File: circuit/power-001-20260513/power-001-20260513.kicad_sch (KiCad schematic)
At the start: 57 parts, among them J1 VIN, J2 +5V_{Line}, J3 Power, J4 Logic, J5 Sub_{Power}, J6 Sub_{Signal}, Q1 BSS138, Q2 PMOS, SW1 SW_SPDT, SW2 SW_SPDT, SW3 SW_SPDT, SW4 Locker_SW, U1 OKL-T/6-W12N-C, U2 OKL-T/6-W12N-C, U3 AZ1084-3.3, U4 BP5293-33, U5 PIC12F683-xSN

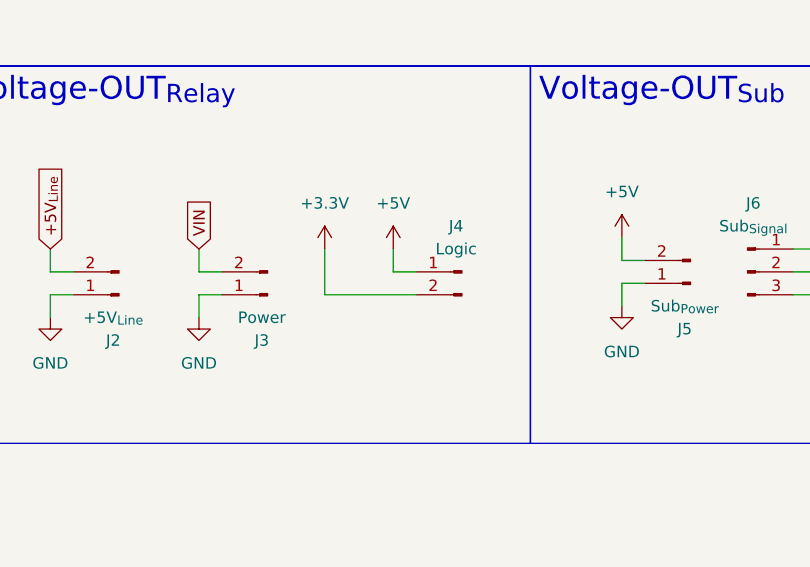
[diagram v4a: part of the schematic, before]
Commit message: Update 供給基板のXT30の向きを変更、それに伴う電源基板の回路図も変更
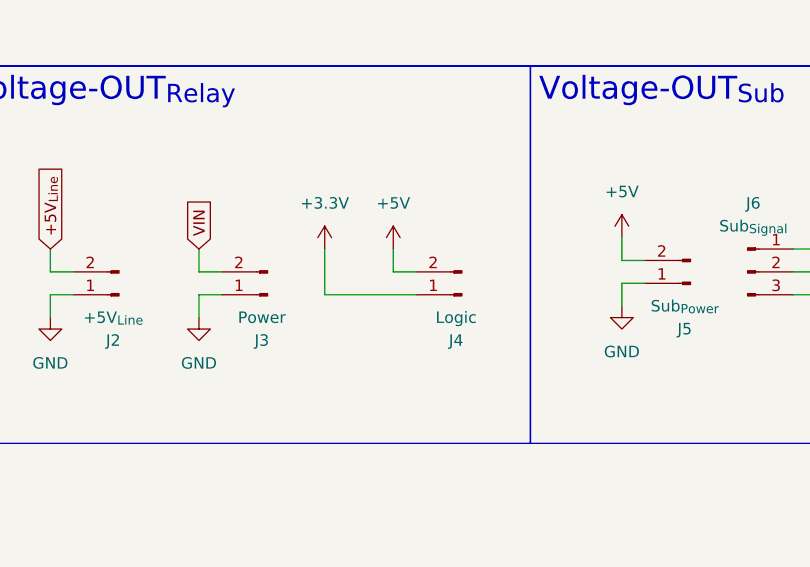
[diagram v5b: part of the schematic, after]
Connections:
- net +3.3V: now also J4.1 (Pin_1); no longer J4.2 (Pin_2)
- net +5V: now also J4.2 (Pin_2); no longer J4.1 (Pin_1)
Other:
- moved on the sheet: J4
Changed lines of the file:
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@@
 	(wire
 		(pts
+			(xy 172.72 121.92) (xy 182.88 121.92)
+		)
+		(stroke
+			(width 0)
+			(type default)
+		)
+	)
+	(wire
+		(pts
 			(xy 226.06 76.2) (xy 223.52 76.2)
 		)
@@
 	(wire
 		(pts
-			(xy 182.88 121.92) (xy 172.72 121.92)
-		)
-		(stroke
-			(width 0)
-			(type default)
-		)
-	)
-	(wire
-		(pts
 			(xy 20.32 125.73) (xy 22.86 125.73)
 		)
@@
 	(symbol
 		(lib_id "Connector:Conn_01x02_Pin")
-		(at 187.96 119.38 0)
-		(mirror y)
+		(at 187.96 121.92 180)
 		(unit 1)
 		(body_style 1)
@@
 		(dnp no)
 		(property "Reference" "J4"
-			(at 187.325 114.3 0)
+			(at 187.325 127 0)
 			(show_name no)
 			(do_not_autoplace no)
@@
 		)
 		(property "Value" "Logic"
-			(at 187.325 116.84 0)
+			(at 187.325 124.46 0)
 			(show_name no)
 			(do_not_autoplace no)
@@
 		)
 		(property "Footprint" "Connector_AMASS:AMASS_XT30PW-F_1x02_P2.50mm_Horizontal"
-			(at 187.96 119.38 0)
+			(at 187.96 121.92 0)
 			(hide yes)
 			(show_name no)
@@
 		)
 		(property "Datasheet" ""
-			(at 187.96 119.38 0)
+			(at 187.96 121.92 0)
 			(hide yes)
 			(show_name no)
@@
 		)
 		(property "Description" "Generic connector, single row, 01x02, script generated"
-			(at 187.96 119.38 0)
+			(at 187.96 121.92 0)
 			(hide yes)
 			(show_name no)
